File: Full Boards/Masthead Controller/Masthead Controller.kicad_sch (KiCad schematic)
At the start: 165 parts, among them Q1 2N7002, Q2 2N7002, SW1 SW_MEC_5G, SW2 SW_MEC_5G

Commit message: Updated schematic and PCB to use the updated symbols and footprints.
Signed-off-by: digimer <digital.mermaid@gmail.com>
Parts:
- CMC1: Part (none) -> TDK ACT12101012PTL00
- TB2, TB3: value Keystone Electronics 7799 -> 7799; Part (none) -> Keystone 7799
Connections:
- net +24V_ISO: no longer TB2.2, TB2.3, TB2.4, TB2.5, TB2.6
- net GND: no longer TB3.2, TB3.3, TB3.4, TB3.5, TB3.6
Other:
- moved on the sheet: TVS1

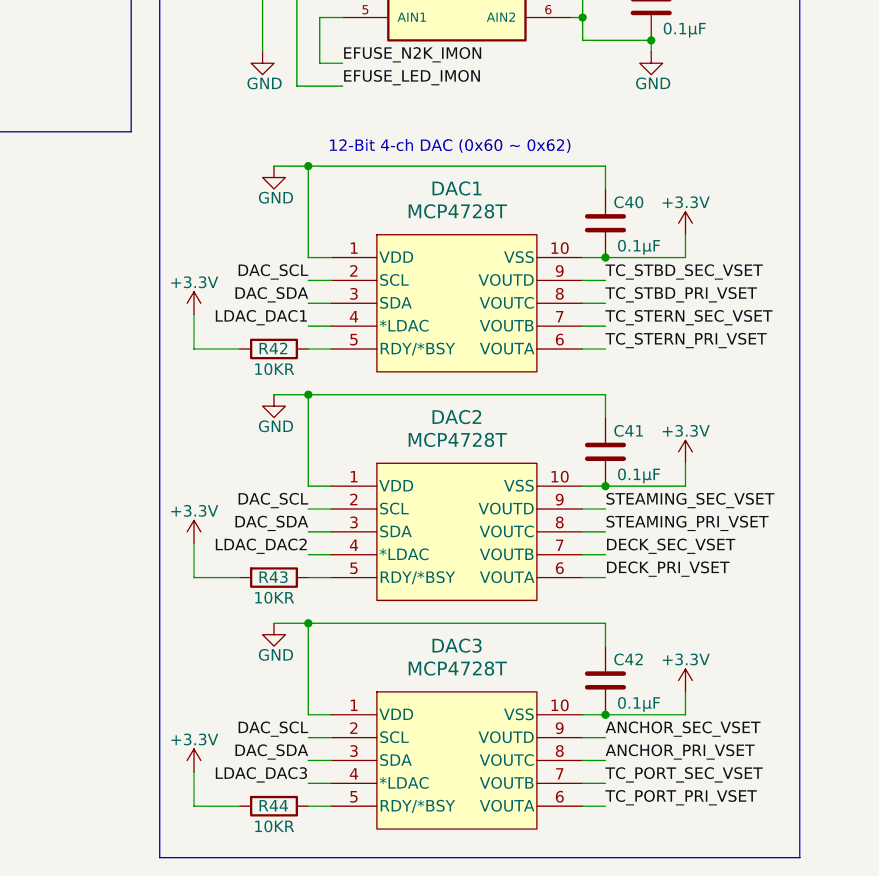
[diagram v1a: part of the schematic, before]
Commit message: Fixed the reversed VSS/VDD pins on the DACs.
Signed-off-by: digimer <digital.mermaid@gmail.com>
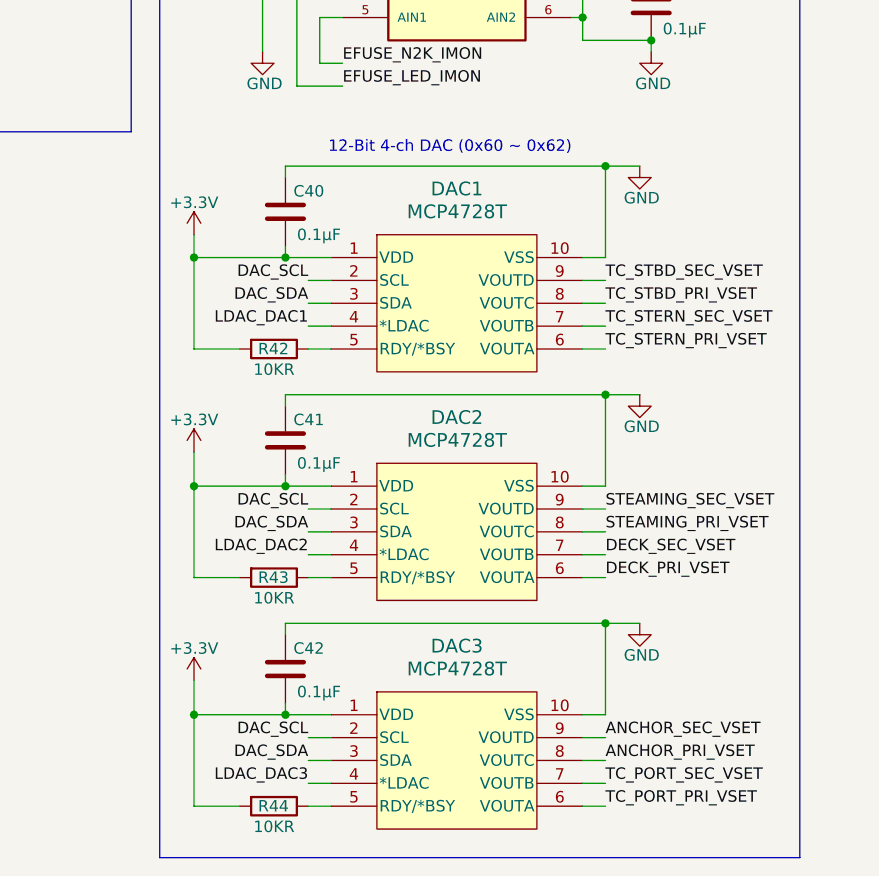
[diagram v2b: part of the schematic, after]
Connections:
- net +3.3V: now also DAC1.1 (VDD), DAC2.1 (VDD), DAC3.1 (VDD); no longer DAC1.10 (VSS), DAC2.10 (VSS), DAC3.10 (VSS)
- net GND: now also DAC1.10 (VSS), DAC2.10 (VSS), DAC3.10 (VSS); no longer DAC1.1 (VDD), DAC2.1 (VDD), DAC3.1 (VDD)

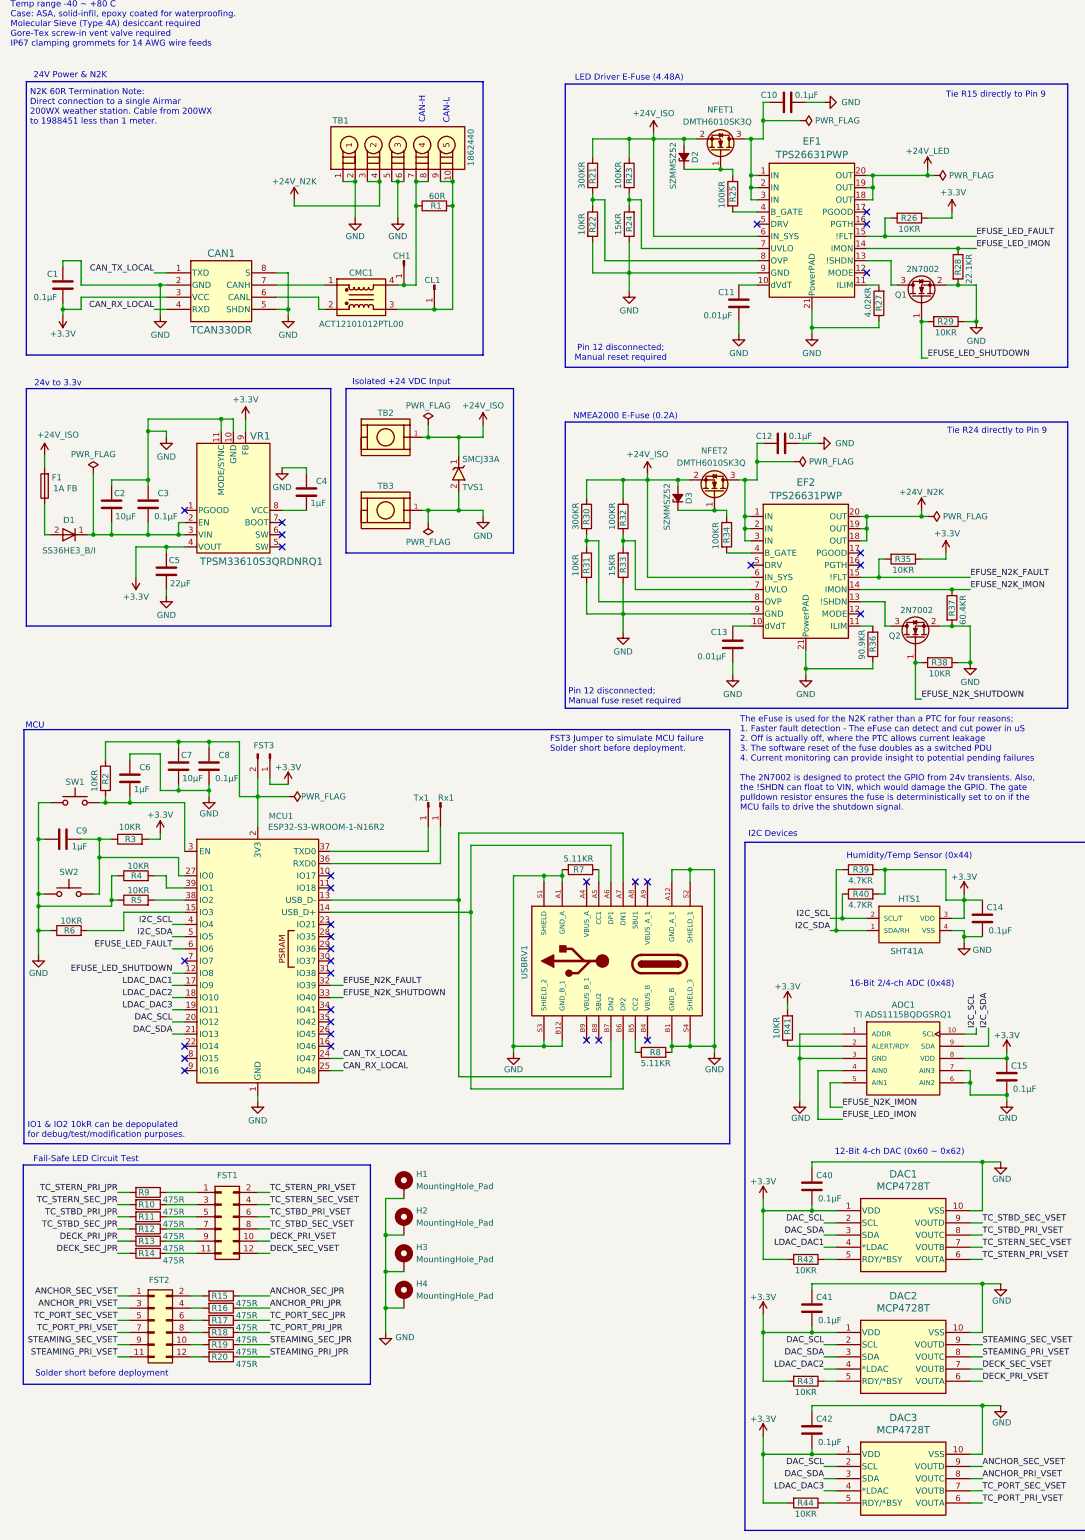
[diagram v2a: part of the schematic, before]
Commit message: Added missing pull-up resistors for the DAC's I2C pins.
Signed-off-by: digimer <digital.mermaid@gmail.com>
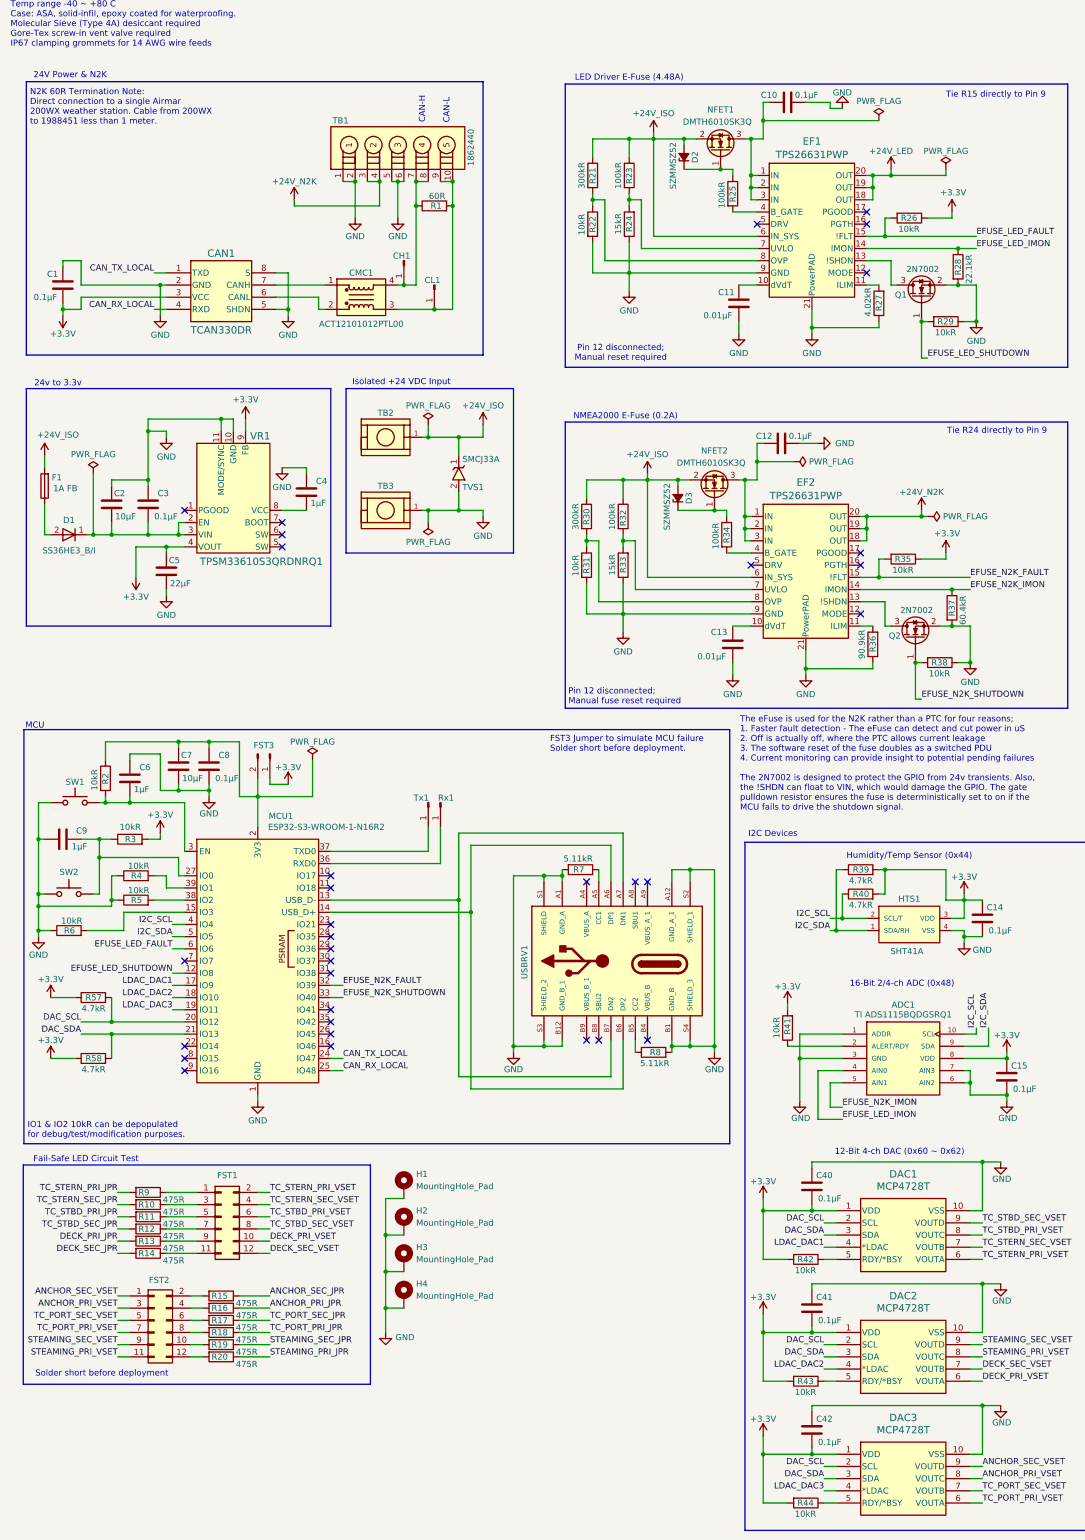
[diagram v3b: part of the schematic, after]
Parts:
- added R57, R58: 4.7kR, mr-stuff:Stackpole_RNCP1206, symbol Device:R
- R2, R22, R26, R29, R3, R31, R35, R38, R4, R41, R42, R43, R44, R5, R6: value 10KR -> 10kR
- R21, R30: value 300KR -> 300kR
- R23, R25, R32, R34: value 100KR -> 100kR
- R24, R33: value 15KR -> 15kR
- R27: value 4.02KR -> 4.02kR
- R28: value 22.1KR -> 22.1kR
- R36: value 90.9KR -> 90.9kR
- R37: value 60.4KR -> 60.4kR
- R39, R40: value 4.7KR -> 4.7kR
- R7, R8: value 5.11KR -> 5.11kR
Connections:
- net +3.3V: now also R57.1, R58.1
- net DAC_SCL: now also R57.2
- net DAC_SDA: now also R58.2

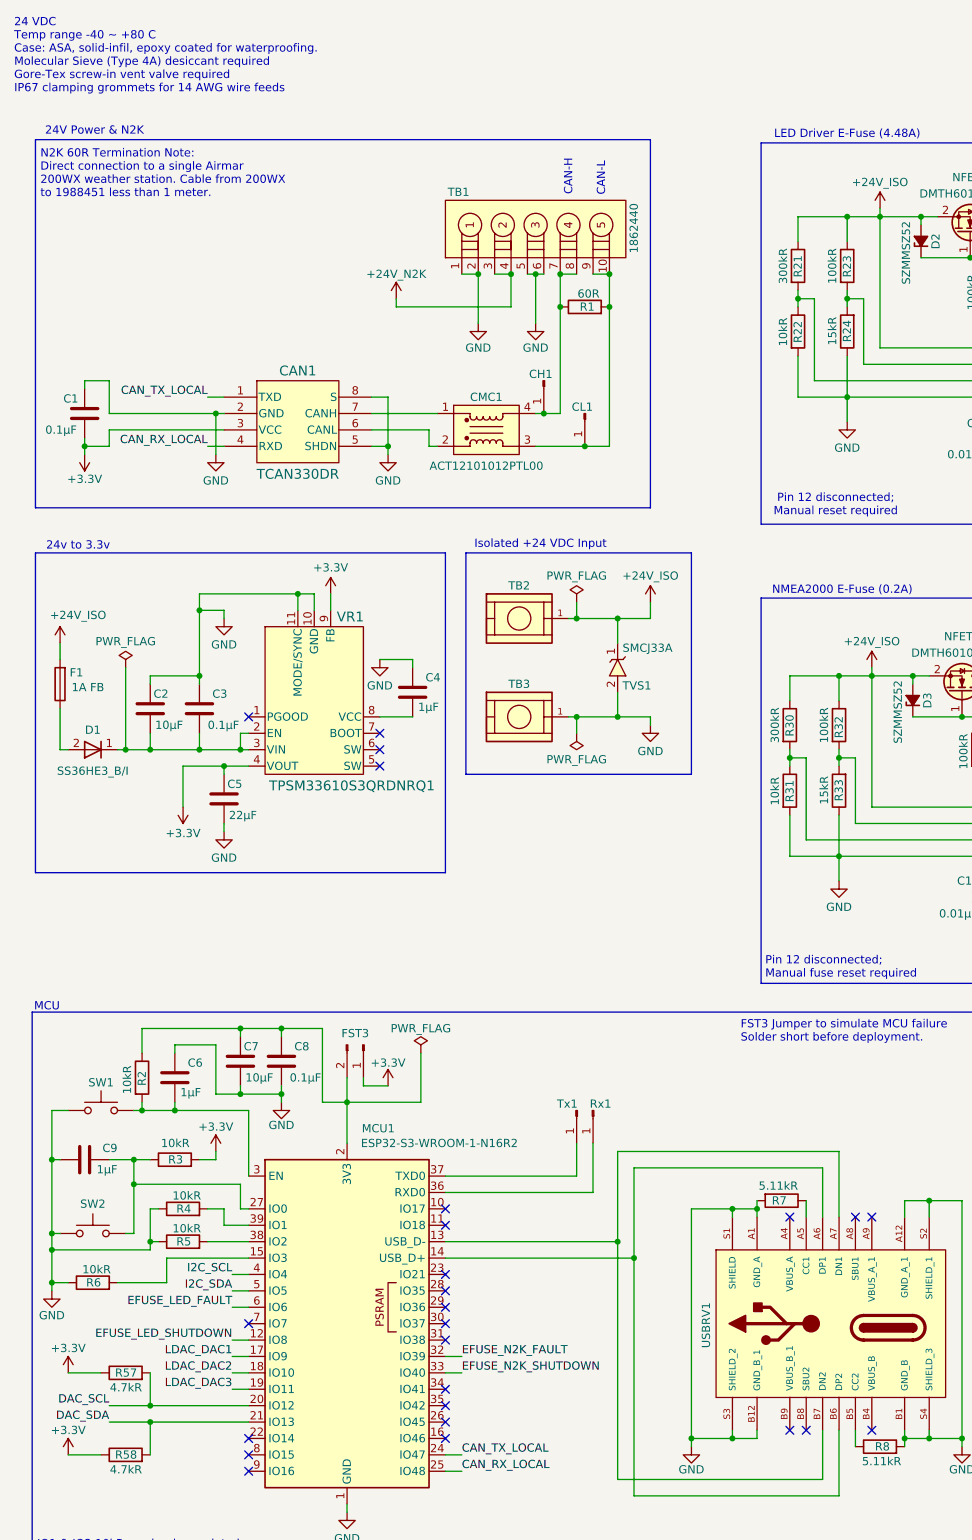
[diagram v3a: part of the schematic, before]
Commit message: Placed the new I2C pull-up resistors and repositioned the transposed resistors on the e-fuses.
Signed-off-by: digimer <digital.mermaid@gmail.com>
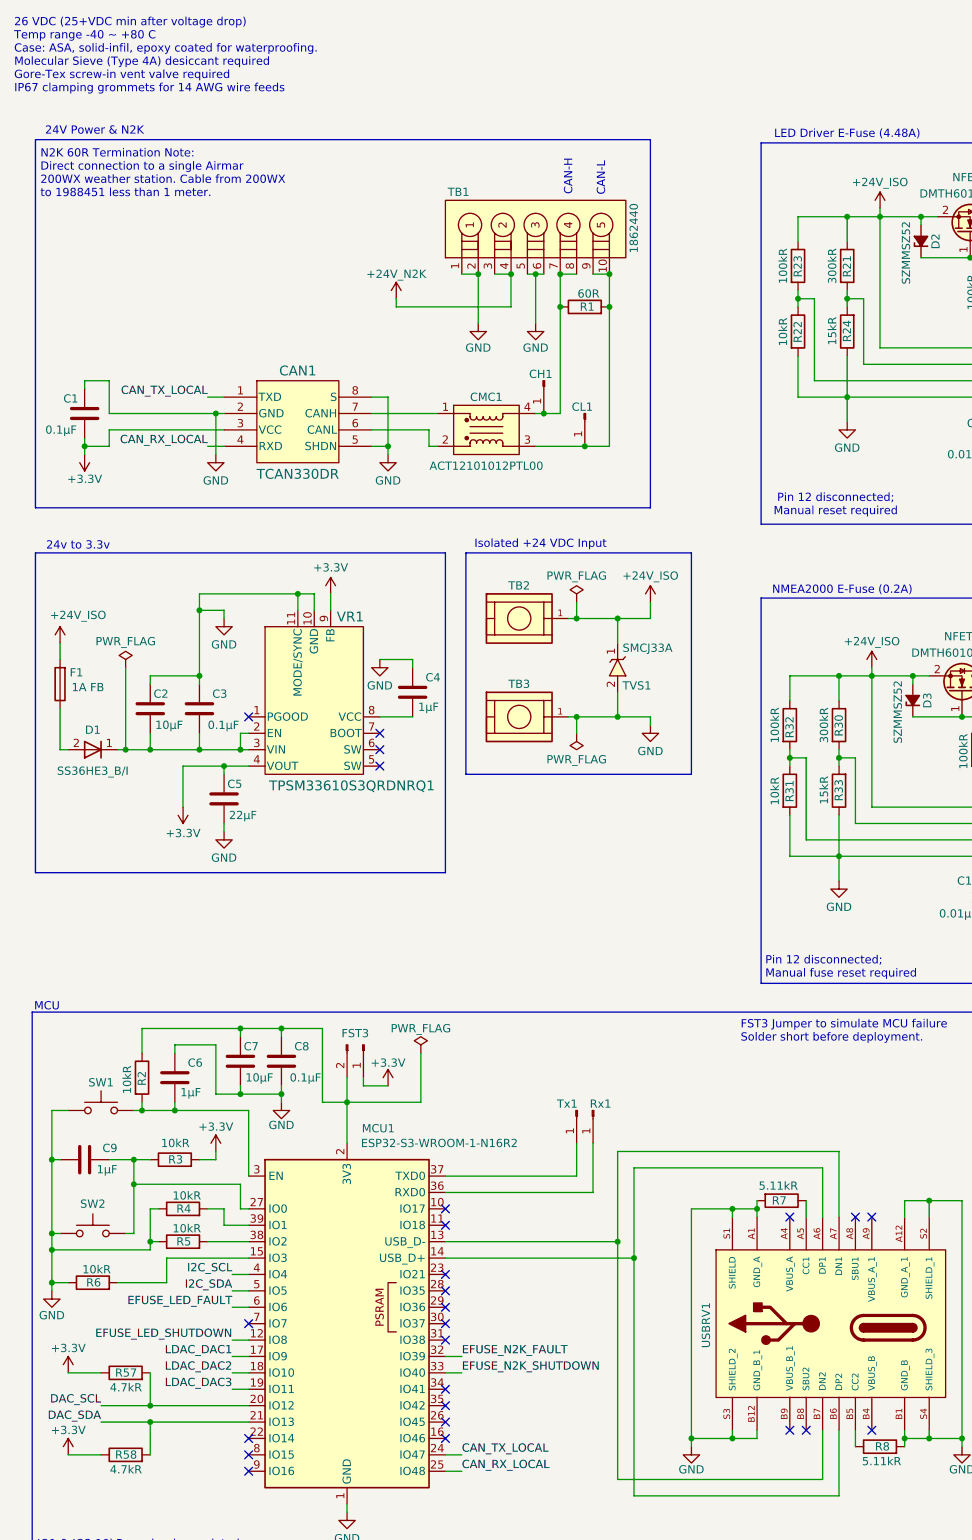
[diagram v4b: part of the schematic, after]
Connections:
- net at EF1.8 (OVP), R22.1: now also R23.2; no longer R21.2
- net at EF2.7 (UVLO), R33.2: now also R30.2; no longer R32.2
- net at EF2.8 (OVP), R31.1: now also R32.2; no longer R30.2
- net at EF1.7 (UVLO), R24.2: now also R21.2; no longer R23.2
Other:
- note added: "26 VDC (25+VDC min after voltage drop) Temp range -40 ~ +80 C Case: ASA, solid-infil, epoxy coated for waterproofing. Molecular Sieve (Type 4A) desiccant required Gore-Tex screw-in vent valve required IP67 clamping grommets for 14 AWG wire feeds"
- note removed: "24 VDC Temp range -40 ~ +80 C Case: ASA, solid-infil, epoxy coated for waterproofing. Molecular Sieve (Type 4A) desiccant required Gore-Tex screw-in vent valve required IP67 clamping grommets for 14 AWG wire feeds"

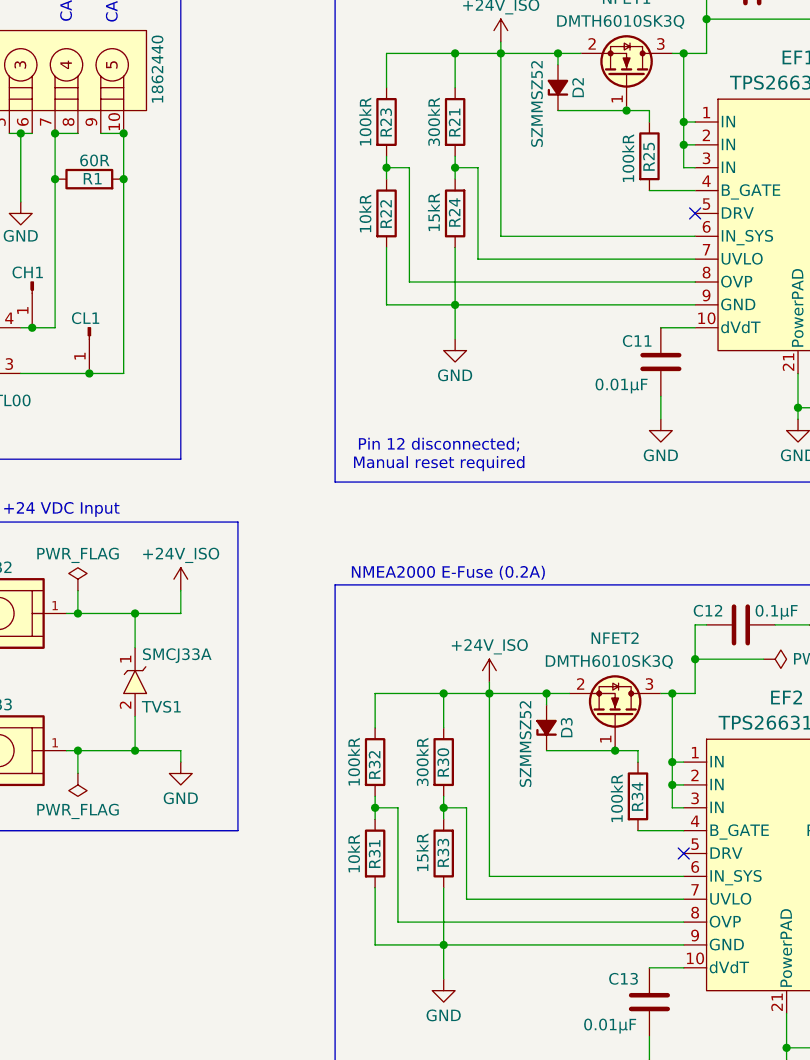
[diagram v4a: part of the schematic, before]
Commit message: Updated the other leg of the voltage dividers for the e-Fuse OVP and UVLO.
Signed-off-by: digimer <digital.mermaid@gmail.com>
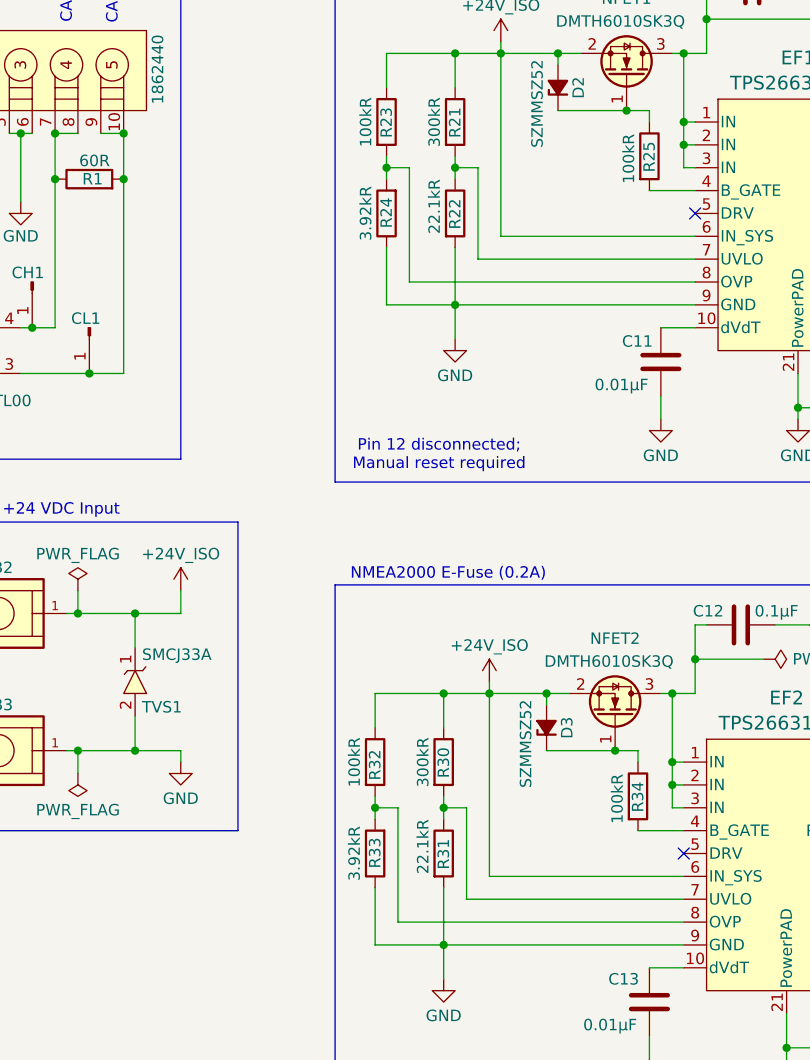
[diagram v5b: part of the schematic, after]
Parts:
- R22, R31: value 10kR -> 22.1kR; Part (none) -> Stackpole RNCP1206FTD22K1
- R24, R33: value 15kR -> 3.92kR; footprint mr-stuff:Stackpole_RNCP1206 -> mr-stuff:Stackpole RMCA0805; Part (none) -> Stackpole RNCP0805FTD3K92
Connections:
- net at EF1.8 (OVP), R23.2: now also R24.2; no longer R22.1
- net at EF2.7 (UVLO), R30.2: now also R31.1; no longer R33.2
- net at EF2.8 (OVP), R32.2: now also R33.2; no longer R31.1
- net at EF1.7 (UVLO), R21.2: now also R22.1; no longer R24.2
